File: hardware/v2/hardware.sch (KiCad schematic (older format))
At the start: 41 parts, among them J1 Screw_Terminal_1x03, J2 Screw_Terminal_01x02, J3 Screw_Terminal_1x03, J4 Barrel_Jack_Switch, J5 Screw_Terminal_01x02, J6 Screw_Terminal_01x02, J7 Screw_Terminal_01x02, P1 CONN_01X02, P2 CONN_01X08, Q0 2n7002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

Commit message: PCB V2
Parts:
- added C6: 100n, Capacitor_SMD:C_0805_2012Metric_Pad1.15x1.40mm_HandSolder, symbol hardware-rescue:C
- added R18: 10k, Resistor_SMD:R_0805_2012Metric_Pad1.15x1.40mm_HandSolder, symbol hardware-rescue:R
- U1: symbol wemos_mini:WeMos_mini -> hardware-rescue:WeMos_mini-wemos_mini
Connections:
- net A0: now also C6.1, R18.1; no longer R12.1, U3.1
- net GND: now also C6.2
- new net: R12.1, R18.2, U3.1
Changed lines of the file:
@@
 $EndDescr
 $Comp
-L wemos_mini:WeMos_mini U1
+L hardware-rescue:WeMos_mini-wemos_mini U1
 U 1 1 5BB7B1E5
 P 1900 1400
@@
 $EndComp
 Wire Wire Line
-	7100 1350 7100 1550
+	7100 1350 7100 1500
 $Comp
 L power:+3.3V #PWR026
@@
 Wire Wire Line
 	7100 650  7100 750
-Text GLabel 6750 1050 0    60   Output ~ 0
+Text GLabel 6700 1050 0    60   Output ~ 0
 A0
 Text GLabel 2750 2000 2    60   Input ~ 0
@@
 	0    -1   -1   0
 $EndComp
-Wire Wire Line
-	6750 1050 7300 1050
-Connection ~ 7300 1050
-Wire Wire Line
-	7300 1050 8000 1050
 $Comp
 L power:+9V #PWR034
@@
 Wire Wire Line
 	8250 1050 8000 1050
-Connection ~ 8000 1050
 Wire Wire Line
 	8000 1050 8000 650
@@
 Wire Wire Line
 	9150 3750 9550 3750
+$Comp
+L hardware-rescue:R R18
+U 1 1 5C9C7BAA
+P 7750 1050
+F 0 "R18" V 7830 1050 50  0000 C CNN
+F 1 "10k" V 7750 1050 50  0000 C CNN
+F 2 "Resistor_SMD:R_0805_2012Metric_Pad1.15x1.40mm_HandSolder" V 7680 1050 50  0001 C CNN
+F 3 "" H 7750 1050 50  0000 C CNN
+	1    7750 1050
+	0    -1   -1   0
+$EndComp
+$Comp
+L hardware-rescue:C C6
+U 1 1 5C9C7C4E
+P 7450 1300
+F 0 "C6" H 7475 1400 50  0000 L CNN
+F 1 "100n" H 7475 1200 50  0000 L CNN
+F 2 "Capacitor_SMD:C_0805_2012Metric_Pad1.15x1.40mm_HandSolder" H 7488 1150 50  0001 C CNN
+F 3 "" H 7450 1300 50  0000 C CNN
+	1    7450 1300
+	1    0    0    -1
+$EndComp
+Wire Wire Line
+	7100 1500 7450 1500
+Wire Wire Line
+	7450 1500 7450 1450
+Connection ~ 7100 1500
+Wire Wire Line
+	7100 1500 7100 1550
+Wire Wire Line
+	7450 1050 7450 1150
+Wire Wire Line
+	7600 1050 7450 1050
+Connection ~ 7450 1050
+Wire Wire Line
+	7900 1050 8000 1050
+Connection ~ 8000 1050
+Wire Wire Line
+	6700 1050 7300 1050
+Connection ~ 7300 1050
+Wire Wire Line
+	7300 1050 7450 1050
 $EndSCHEMATC

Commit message: Added pressure sensor
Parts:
- R12, R13, R14, R15, R16, R17, R18: footprint Resistor_SMD:R_0805_2012Metric_Pad1.15x1.40mm_HandSolder -> Resistor_SMD:R_1206_3216Metric_Pad1.42x1.75mm_HandSolder
- U3: footprint Package_DIP:DIP-8_W8.89mm_SMDSocket_LongPads -> Package_SO:SOIC-8_3.9x4.9mm_P1.27mm
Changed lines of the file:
@@
 F 0 "R17" V 10280 1750 50  0000 C CNN
 F 1 "680" V 10200 1750 50  0000 C CNN
-F 2 "Resistor_SMD:R_0805_2012Metric_Pad1.15x1.40mm_HandSolder" V 10130 1750 50  0001 C CNN
+F 2 "Resistor_SMD:R_1206_3216Metric_Pad1.42x1.75mm_HandSolder" V 10130 1750 50  0001 C CNN
 F 3 "" H 10200 1750 50  0000 C CNN
 	1    10200 1750
@@
 F 0 "R16" V 10030 1750 50  0000 C CNN
 F 1 "680" V 9950 1750 50  0000 C CNN
-F 2 "Resistor_SMD:R_0805_2012Metric_Pad1.15x1.40mm_HandSolder" V 9880 1750 50  0001 C CNN
+F 2 "Resistor_SMD:R_1206_3216Metric_Pad1.42x1.75mm_HandSolder" V 9880 1750 50  0001 C CNN
 F 3 "" H 9950 1750 50  0000 C CNN
 	1    9950 1750
@@
 F 0 "U3" H 8550 1417 50  0000 C CNN
 F 1 "LM358" H 8550 1326 50  0000 C CNN
-F 2 "Package_DIP:DIP-8_W8.89mm_SMDSocket_LongPads" H 8550 1050 50  0001 C CNN
+F 2 "Package_SO:SOIC-8_3.9x4.9mm_P1.27mm" H 8550 1050 50  0001 C CNN
 F 3 "http://www.ti.com/lit/ds/symlink/lm2904-n.pdf" H 8550 1050 50  0001 C CNN
 	1    8550 1050
@@
 F 0 "R14" V 9180 950 50  0000 C CNN
 F 1 "20k" V 9100 950 50  0000 C CNN
-F 2 "Resistor_SMD:R_0805_2012Metric_Pad1.15x1.40mm_HandSolder" V 9030 950 50  0001 C CNN
+F 2 "Resistor_SMD:R_1206_3216Metric_Pad1.42x1.75mm_HandSolder" V 9030 950 50  0001 C CNN
 F 3 "" H 9100 950 50  0000 C CNN
 	1    9100 950
@@
 F 0 "R15" V 9180 1150 50  0000 C CNN
 F 1 "20k" V 9100 1150 50  0000 C CNN
-F 2 "Resistor_SMD:R_0805_2012Metric_Pad1.15x1.40mm_HandSolder" V 9030 1150 50  0001 C CNN
+F 2 "Resistor_SMD:R_1206_3216Metric_Pad1.42x1.75mm_HandSolder" V 9030 1150 50  0001 C CNN
 F 3 "" H 9100 1150 50  0000 C CNN
 	1    9100 1150
@@
 F 0 "R13" V 8980 1500 50  0000 C CNN
 F 1 "10k" V 8900 1500 50  0000 C CNN
-F 2 "Resistor_SMD:R_0805_2012Metric_Pad1.15x1.40mm_HandSolder" V 8830 1500 50  0001 C CNN
+F 2 "Resistor_SMD:R_1206_3216Metric_Pad1.42x1.75mm_HandSolder" V 8830 1500 50  0001 C CNN
 F 3 "" H 8900 1500 50  0000 C CNN
 	1    8900 1500
@@
 F 0 "R12" V 8530 650 50  0000 C CNN
 F 1 "10k" V 8450 650 50  0000 C CNN
-F 2 "Resistor_SMD:R_0805_2012Metric_Pad1.15x1.40mm_HandSolder" V 8380 650 50  0001 C CNN
+F 2 "Resistor_SMD:R_1206_3216Metric_Pad1.42x1.75mm_HandSolder" V 8380 650 50  0001 C CNN
 F 3 "" H 8450 650 50  0000 C CNN
 	1    8450 650
@@
 F 0 "R18" V 7830 1050 50  0000 C CNN
 F 1 "10k" V 7750 1050 50  0000 C CNN
-F 2 "Resistor_SMD:R_0805_2012Metric_Pad1.15x1.40mm_HandSolder" V 7680 1050 50  0001 C CNN
+F 2 "Resistor_SMD:R_1206_3216Metric_Pad1.42x1.75mm_HandSolder" V 7680 1050 50  0001 C CNN
 F 3 "" H 7750 1050 50  0000 C CNN
 	1    7750 1050

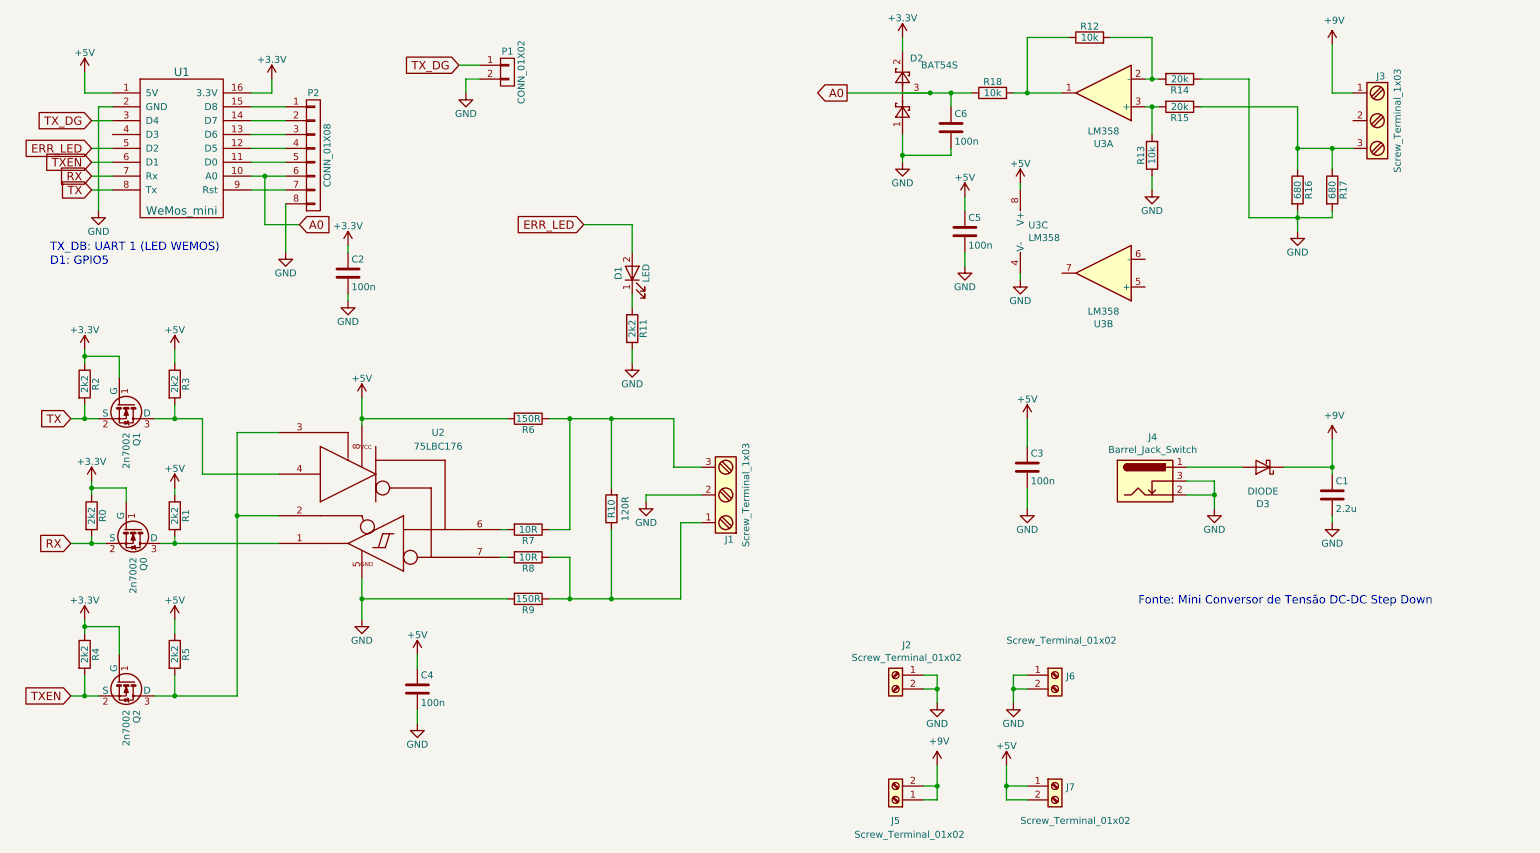
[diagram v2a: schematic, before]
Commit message: Corrected offset and display pressure in kgfm/cm2
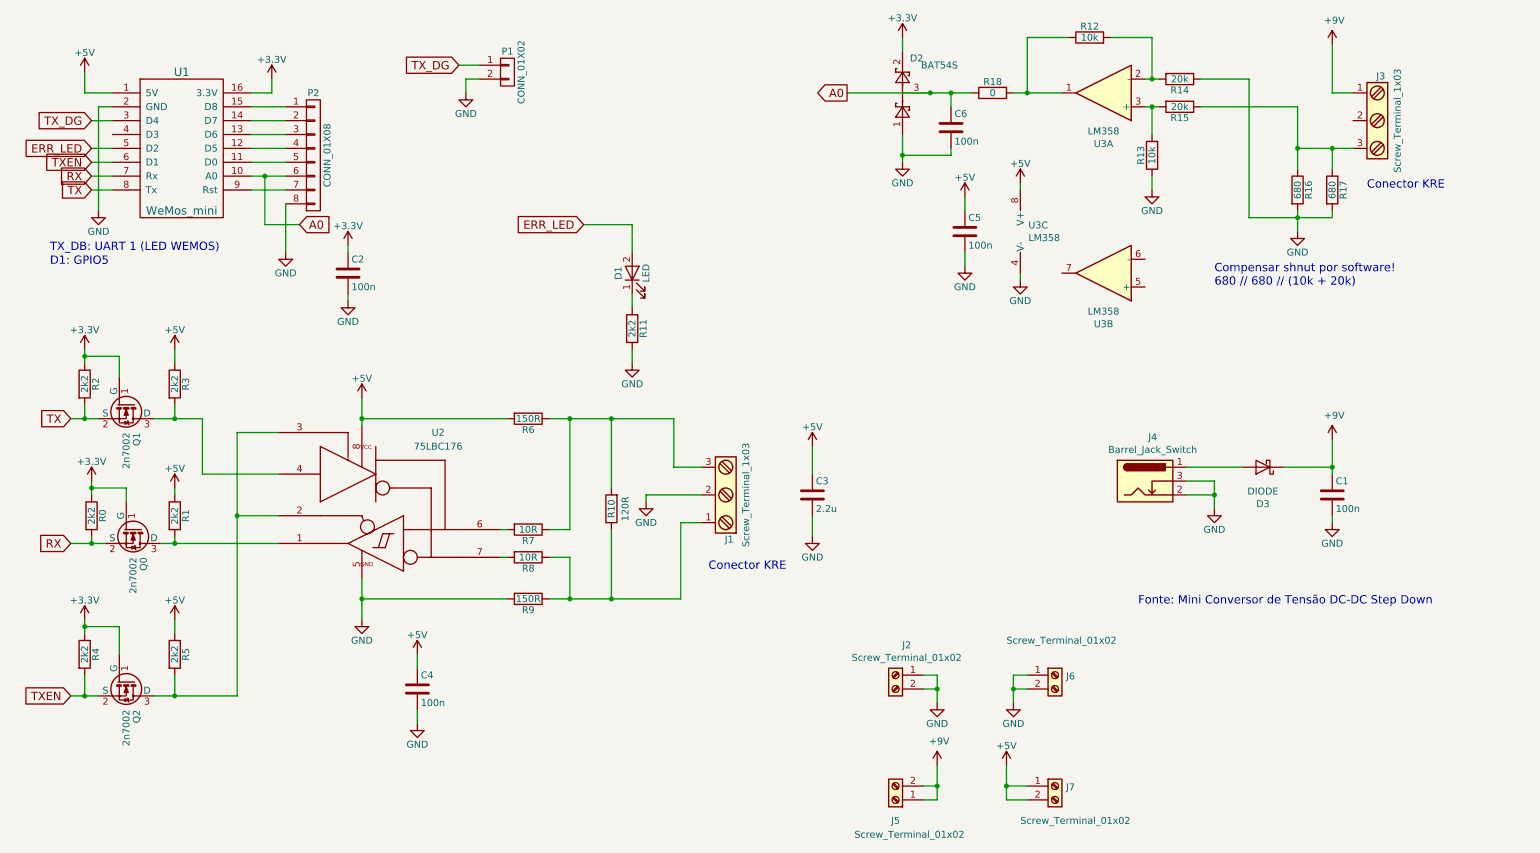
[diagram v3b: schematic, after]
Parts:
- C1: value 2.2u -> 100n
- C3: value 100n -> 2.2u; footprint Capacitor_SMD:C_1206_3216Metric_Pad1.42x1.75mm_HandSolder -> Capacitor_SMD:C_0805_2012Metric_Pad1.15x1.40mm_HandSolder
- R18: value 10k -> 0
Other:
- note added: "Compensar shnut por software!\n680 // 680 // (10k + 20k)"
- note added: "Conector KRE"
- moved on the sheet: C3
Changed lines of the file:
@@
 P 10200 3950
 F 0 "C1" H 10225 4050 50  0000 L CNN
-F 1 "2.2u" H 10225 3850 50  0000 L CNN
+F 1 "100n" H 10225 3850 50  0000 L CNN
 F 2 "Capacitor_SMD:C_0805_2012Metric_Pad1.15x1.40mm_HandSolder" H 10238 3800 50  0001 C CNN
 F 3 "" H 10200 3950 50  0000 C CNN
@@
 Connection ~ 7850 6050
 Wire Wire Line
-	8000 3900 8000 4050
-$Comp
-L power:GND #PWR023
-U 1 1 5BBD1A56
-P 8000 4050
-F 0 "#PWR023" H 8000 3800 50  0001 C CNN
-F 1 "GND" H 8000 3900 50  0000 C CNN
-F 2 "" H 8000 4050 50  0000 C CNN
-F 3 "" H 8000 4050 50  0000 C CNN
-	1    8000 4050
-	1    0    0    -1
-$EndComp
-Wire Wire Line
-	8000 3400 8000 3600
-$Comp
-L power:+5V #PWR022
-U 1 1 5BBD18F8
-P 8000 3400
-F 0 "#PWR022" H 8000 3250 50  0001 C CNN
-F 1 "+5V" H 8000 3540 50  0000 C CNN
-F 2 "" H 8000 3400 50  0000 C CNN
-F 3 "" H 8000 3400 50  0000 C CNN
-	1    8000 3400
-	1    0    0    -1
-$EndComp
-$Comp
-L hardware-rescue:C C3
-U 1 1 5BBD17B0
-P 8000 3750
-F 0 "C3" H 8025 3850 50  0000 L CNN
-F 1 "100n" H 8025 3650 50  0000 L CNN
-F 2 "Capacitor_SMD:C_1206_3216Metric_Pad1.42x1.75mm_HandSolder" H 8038 3600 50  0001 C CNN
-F 3 "" H 8000 3750 50  0000 C CNN
-	1    8000 3750
-	1    0    0    -1
-$EndComp
-Wire Wire Line
 	9850 3750 10200 3750
 Wire Wire Line
@@
 P 7750 1050
 F 0 "R18" V 7830 1050 50  0000 C CNN
-F 1 "10k" V 7750 1050 50  0000 C CNN
+F 1 "0" V 7750 1050 50  0000 C CNN
 F 2 "Resistor_SMD:R_1206_3216Metric_Pad1.42x1.75mm_HandSolder" V 7680 1050 50  0001 C CNN
 F 3 "" H 7750 1050 50  0000 C CNN
@@
 Wire Wire Line
 	7300 1050 7450 1050
+Text Notes 10450 1750 0    60   ~ 0
+Conector KRE
+Text Notes 5700 4500 0    60   ~ 0
+Conector KRE
+Text Notes 9350 2450 0    60   ~ 0
+Compensar shnut por software!\n680 // 680 // (10k + 20k)
+$Comp
+L hardware-rescue:C C3
+U 1 1 5BBD17B0
+P 6450 3950
+F 0 "C3" H 6475 4050 50  0000 L CNN
+F 1 "2.2u" H 6475 3850 50  0000 L CNN
+F 2 "Capacitor_SMD:C_0805_2012Metric_Pad1.15x1.40mm_HandSolder" H 6488 3800 50  0001 C CNN
+F 3 "" H 6450 3950 50  0000 C CNN
+	1    6450 3950
+	1    0    0    -1
+$EndComp
+$Comp
+L power:+5V #PWR022
+U 1 1 5BBD18F8
+P 6450 3600
+F 0 "#PWR022" H 6450 3450 50  0001 C CNN
+F 1 "+5V" H 6450 3740 50  0000 C CNN
+F 2 "" H 6450 3600 50  0000 C CNN
+F 3 "" H 6450 3600 50  0000 C CNN
+	1    6450 3600
+	1    0    0    -1
+$EndComp
+Wire Wire Line
+	6450 3600 6450 3800
+$Comp
+L power:GND #PWR023
+U 1 1 5BBD1A56
+P 6450 4250
+F 0 "#PWR023" H 6450 4000 50  0001 C CNN
+F 1 "GND" H 6450 4100 50  0000 C CNN
+F 2 "" H 6450 4250 50  0000 C CNN
+F 3 "" H 6450 4250 50  0000 C CNN
+	1    6450 4250
+	1    0    0    -1
+$EndComp
+Wire Wire Line
+	6450 4100 6450 4250
 $EndSCHEMATC

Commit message: Board texts
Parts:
- added H1, H2, H3: MountingHole, MountingHole:MountingHole_2.2mm_M2, symbol Mechanical:MountingHole
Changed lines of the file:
@@
 Wire Wire Line
 	6450 4100 6450 4250
+$Comp
+L Mechanical:MountingHole H1
+U 1 1 5CD38FDD
+P 5200 800
+F 0 "H1" H 5300 846 50  0000 L CNN
+F 1 "MountingHole" H 5300 755 50  0000 L CNN
+F 2 "MountingHole:MountingHole_2.2mm_M2" H 5200 800 50  0001 C CNN
+F 3 "~" H 5200 800 50  0001 C CNN
+	1    5200 800
+	1    0    0    -1
+$EndComp
+$Comp
+L Mechanical:MountingHole H2
+U 1 1 5CD39235
+P 5200 1250
+F 0 "H2" H 5300 1296 50  0000 L CNN
+F 1 "MountingHole" H 5300 1205 50  0000 L CNN
+F 2 "MountingHole:MountingHole_2.2mm_M2" H 5200 1250 50  0001 C CNN
+F 3 "~" H 5200 1250 50  0001 C CNN
+	1    5200 1250
+	1    0    0    -1
+$EndComp
+$Comp
+L Mechanical:MountingHole H3
+U 1 1 5CD3932A
+P 5850 1000
+F 0 "H3" H 5950 1046 50  0000 L CNN
+F 1 "MountingHole" H 5950 955 50  0000 L CNN
+F 2 "MountingHole:MountingHole_2.2mm_M2" H 5850 1000 50  0001 C CNN
+F 3 "~" H 5850 1000 50  0001 C CNN
+	1    5850 1000
+	1    0    0    -1
+$EndComp
 $EndSCHEMATC
